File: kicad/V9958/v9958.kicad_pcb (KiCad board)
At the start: 2 copper layers, 160 x 100.3 mm, 5 parts, among them P5 CONN_02X25

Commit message: rca jacks, rough layout test
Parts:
- added C1: 22p, Capacitors_ThroughHole:C_Disc_D3_P2.5, F.Cu at (141.0, 97.8)
- added C10: 100n, Capacitors_ThroughHole:C_Disc_D3_P2.5, F.Cu at (179.1, 109.2)
- added C11: 47µF, Capacitors_ThroughHole:C_Radial_D5_L11_P2.5, F.Cu at (128.3, 105.4)
- added C12: 100n, Capacitors_ThroughHole:C_Disc_D3_P2.5, F.Cu at (179.1, 111.8)
- added C13: 100n, Capacitors_ThroughHole:C_Disc_D3_P2.5, F.Cu at (128.3, 101.6)
- added C14: 220µF, Capacitors_ThroughHole:C_Radial_D6.3_L11.2_P2.5, F.Cu at (85.1, 120.7)
- added C15: 220µF, Capacitors_ThroughHole:C_Radial_D6.3_L11.2_P2.5, F.Cu at (85.1, 78.7)
- added C16: 220µF, Capacitors_ThroughHole:C_Radial_D6.3_L11.2_P2.5, F.Cu at (85.1, 128.3)
- added C17: 47µF, Capacitors_ThroughHole:C_Radial_D5_L11_P2.5, F.Cu at (110.5, 81.3)
- added C18: 220µF, Capacitors_ThroughHole:C_Radial_D6.3_L11.2_P2.5, F.Cu at (85.1, 109.2)
- added C19: 100n, Capacitors_ThroughHole:C_Disc_D3_P2.5, F.Cu at (113.0, 86.4)
- added C2: 22p, Capacitors_ThroughHole:C_Disc_D3_P2.5, F.Cu at (141.0, 82.5)
- added C20: 220µF, Capacitors_ThroughHole:C_Radial_D6.3_L11.2_P2.5, F.Cu at (85.1, 63.5)
- added C21: 220µF, Capacitors_ThroughHole:C_Radial_D6.3_L11.2_P2.5, F.Cu at (85.1, 94.0)
- added C3: 100n, Capacitors_ThroughHole:C_Disc_D3_P2.5, F.Cu at (147.3, 80.0)
- added C4: 100n, Capacitors_ThroughHole:C_Disc_D3_P2.5, F.Cu at (160.0, 80.0)
- added C5: 100n, Capacitors_ThroughHole:C_Disc_D3_P2.5, F.Cu at (172.7, 80.0)
- added C6: 100n, Capacitors_ThroughHole:C_Disc_D3_P2.5, F.Cu at (185.4, 80.0)
- added C7: 100n, Capacitors_ThroughHole:C_Disc_D3_P2.5, F.Cu at (208.3, 108.0)
- added C8: 100n, Capacitors_ThroughHole:C_Disc_D3_P2.5, F.Cu at (158.8, 87.6)
- added C9: 100n, Capacitors_ThroughHole:C_Disc_D3_P2.5, F.Cu at (179.1, 114.3)
- added JP1: JUMPER, Pin_Headers:Pin_Header_Straight_1x02, F.Cu at (210.8, 91.4)
- added P1: RCA JACK, w_conn_av:rca_black, F.Cu at (71.1, 78.7)
- added P2: RCA JACK, w_conn_av:rca_black, F.Cu at (71.1, 109.2)
- added P3: RCA JACK, w_conn_av:rca_black, F.Cu at (71.1, 63.5)
- added P4: RCA JACK, w_conn_av:rca_black, F.Cu at (71.1, 94.0)
- added R1: 470, Resistors_ThroughHole:Resistor_Horizontal_RM10mm, F.Cu at (186.7, 119.4)
- added R10: 2.61k/10%, Resistors_ThroughHole:Resistor_Horizontal_RM10mm, F.Cu at (120.7, 82.5)
- added R11: 75, Resistors_ThroughHole:Resistor_Horizontal_RM10mm, F.Cu at (99.1, 124.5)
- added R12: 75, Resistors_ThroughHole:Resistor_Horizontal_RM10mm, F.Cu at (99.1, 120.7)
- added R13: 240, Resistors_ThroughHole:Resistor_Horizontal_RM10mm, F.Cu at (90.2, 96.5)
- added R2: 470, Resistors_ThroughHole:Resistor_Horizontal_RM10mm, F.Cu at (182.9, 119.4)
- added R3: 470, Resistors_ThroughHole:Resistor_Horizontal_RM10mm, F.Cu at (190.5, 119.4)
- added R4: 2.2k, Resistors_ThroughHole:Resistor_Horizontal_RM10mm, F.Cu at (124.5, 105.4)
- added R5: 2.2k, Resistors_ThroughHole:Resistor_Horizontal_RM10mm, F.Cu at (137.2, 104.1)
- added R6: 75, Resistors_ThroughHole:Resistor_Horizontal_RM10mm, F.Cu at (101.0, 78.7)
- added R7: 75, Resistors_ThroughHole:Resistor_Horizontal_RM10mm, F.Cu at (100.3, 109.2)
- added R8: 75, Resistors_ThroughHole:Resistor_Horizontal_RM10mm, F.Cu at (100.3, 63.5)
- added R9: 43, Resistors_ThroughHole:Resistor_Horizontal_RM10mm, F.Cu at (100.3, 92.7)
- added U1: 7400, Housings_DIP:DIP-14_W7.62mm_LongPads, F.Cu at (200.7, 111.8)
- added U2: V9958, SDIP:SDIP64, F.Cu at (175.3, 94.0)
- added U3: DRAM_64KX4, Housings_DIP:DIP-18_W7.62mm_LongPads, F.Cu at (147.3, 55.9)
- added U4: DRAM_64KX4, Housings_DIP:DIP-18_W7.62mm_LongPads, F.Cu at (160.0, 55.9)
- added U5: DRAM_64KX4, Housings_DIP:DIP-18_W7.62mm_LongPads, F.Cu at (172.7, 55.9)
- added U6: DRAM_64KX4, Housings_DIP:DIP-18_W7.62mm_LongPads, F.Cu at (185.4, 55.9)
- added U7: cxa2075M, Housings_SOIC:SOIC-24_7.5x15.4mm_Pitch1.27mm, F.Cu at (118.1, 94.0)
- added X1: OSC, Oscillators:KXO-200_LargePads, F.Cu at (116.8, 115.6)
- added X2: MINI_DIN_4, mini_din:mini_din-M_DIN4, F.Cu at (66.0, 124.5)
- added Y1: 21,443Mhz, Crystals:Crystal_HC49-U_Vertical, F.Cu at (142.2, 90.2)
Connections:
- net /CSW_VDP renamed /50pin connector/A5
- net /CS_RES02 renamed /CS_IO1
- net /Connector/A2 renamed /50pin connector/A2
- net /Connector/A3 renamed /50pin connector/A3
- net /Connector/A4 renamed /50pin connector/A4
- net /Connector/D0 renamed Net-(P5-Pad14)
- net /WE2 renamed /50pin connector/RESET_TRIG
- net E_LCD renamed /CS_IO0
- net Net-(P5-Pad19) renamed /CS_IO2
- P5 pad 10: /Connector/D4 -> /50pin connector/D3
- P5 pad 11: /Connector/D3 -> /50pin connector/D2
- P5 pad 12: /Connector/D2 -> /50pin connector/D1
- P5 pad 13: /Connector/D1 -> /50pin connector/D0
- P5 pad 15: Net-(P5-Pad15) -> /RW
- P5 pad 16: /RW -> Net-(P5-Pad16)
- P5 pad 17: Net-(P5-Pad17) -> RDY
- P5 pad 18: RDY -> Net-(P5-Pad18)
- P5 pad 24: /CSR_VDP -> /CS_VDP
- P5 pad 29: /Connector/A1 -> /50pin connector/A1
- P5 pad 30: /Connector/A0 -> /50pin connector/A0
- P5 pad 35: PHI2 -> GND
- P5 pad 36: Net-(P5-Pad36) -> PHI2
- P5 pad 37: /OE2 -> GND
- P5 pad 43: Net-(P5-Pad43) -> VCC
- P5 pad 44: Net-(P5-Pad44) -> VCC
- P5 pad 45: Net-(P5-Pad45) -> VCC
- P5 pad 46: Net-(P5-Pad46) -> VCC
- P5 pad 47: Net-(P5-Pad47) -> GND
- P5 pad 48: Net-(P5-Pad48) -> GND
- P5 pad 49: Net-(P5-Pad49) -> GND
- P5 pad 50: Net-(P5-Pad50) -> GND
- P5 pad 6: Net-(P5-Pad6) -> /50pin connector/D7
- P5 pad 7: /Connector/D7 -> /50pin connector/D6
- P5 pad 8: /Connector/D6 -> /50pin connector/D5
- P5 pad 9: /Connector/D5 -> /50pin connector/D4
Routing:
- net //CAS1: track 0.00 -> 64.1 mm, vias 0 -> 2
- net //RAS: track 0.00 -> 61.2 mm
- net /50pin connector/D7: track 0.00 -> 46.9 mm, vias 0 -> 1
- net /A2: track 0.00 -> 41.3 mm
- net /50pin connector/A1: track 0.00 -> 41.3 mm
- net /50pin connector/A0: track 0.00 -> 41.3 mm
- net /A3: track 0.00 -> 41.2 mm
- net /A5: track 0.00 -> 41.2 mm
- net /A7: track 0.00 -> 41.1 mm
- net /A6: track 0.00 -> 41.0 mm
- net /R/W: track 0.00 -> 41.0 mm
- net /A4: track 0.00 -> 41.0 mm
- net //CAS0: track 0.00 -> 38.2 mm
- net /50pin connector/D1: track 0.00 -> 30.9 mm, vias 0 -> 1
- net /50pin connector/D3: track 0.00 -> 30.0 mm, vias 0 -> 1
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
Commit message: cleanup
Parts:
- P1: value RCA JACK -> RED
- P2: value RCA JACK -> GREEN
- P3: value RCA JACK -> BLUE
- P4: value RCA JACK -> SYNC/C
- R1, R10, R11, R12, R13, R2, R3, R4, R5, R6, R7, R8, R9: footprint Resistors_ThroughHole:Resistor_Horizontal_RM10mm -> Discret:R3
- moved C11 85.4 mm to (95.2, 184.2)
- moved C13 85.4 mm to (95.2, 180.3)
- moved C19 85.4 mm to (80.0, 165.1)
- moved R10 85.4 mm to (87.6, 161.3)
- moved R4 85.4 mm to (91.4, 184.2)
- moved C17 82.5 mm to (96.5, 162.6)
- moved C10 81.3 mm to (115.6, 160.0)
- moved C12 81.3 mm to (115.6, 162.6)
- moved C9 81.3 mm to (115.6, 165.1)
- moved R1 81.3 mm to (123.2, 170.2)
- moved R2 81.3 mm to (119.4, 170.2)
- moved R3 81.3 mm to (127.0, 170.2)
- moved C4 49.1 mm to (111.8, 88.9)
- moved C5 49.1 mm to (124.5, 88.9)
- moved C3 49.1 mm to (99.1, 88.9)
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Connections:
- net /A2 renamed /AD2
- net /A3 renamed /AD3
- net /A4 renamed /AD4
- net /A5 renamed /AD5
- net /A6 renamed /AD6
- net /A7 renamed /AD7
- U2 pad 49: /50pin connector/A0 -> /AD0
- U2 pad 50: /50pin connector/A1 -> /AD1
- U3 pad 13: /50pin connector/A1 -> /AD1
- U3 pad 14: /50pin connector/A0 -> /AD0
- U4 pad 13: /50pin connector/A1 -> /AD1
- U4 pad 14: /50pin connector/A0 -> /AD0
- U5 pad 13: /50pin connector/A1 -> /AD1
- U5 pad 14: /50pin connector/A0 -> /AD0
- U6 pad 13: /50pin connector/A1 -> /AD1
- U6 pad 14: /50pin connector/A0 -> /AD0
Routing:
- net VCC: track 10.0 -> 99.8 mm
- net /AD1: track 0.00 -> 83.8 mm, vias 0 -> 1
- net /AD0: track 0.00 -> 82.2 mm, vias 0 -> 1
- net /RESET: track 0.00 -> 64.3 mm, vias 0 -> 1
- net /AD4: track 41.0 -> 88.7 mm, vias 0 -> 1
- net /AD5: track 41.2 -> 85.0 mm, vias 0 -> 1
- net /AD2: track 41.3 -> 84.1 mm, vias 0 -> 1
- net /AD3: track 41.2 -> 83.9 mm, vias 0 -> 1
- net /AD6: track 41.0 -> 81.6 mm, vias 0 -> 1
- net /IRQ: track 0.00 -> 38.7 mm, vias 0 -> 1
- net /AD7: track 41.1 -> 78.5 mm, vias 0 -> 1
- net //CAS1: track 64.1 -> 28.5 mm, vias 2 -> 0
- net /R/W: track 41.0 -> 70.8 mm
- net /50pin connector/D7: track 46.9 -> 18.3 mm, vias 1 -> 0
- net /RD1: track 28.5 -> 0.00 mm
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
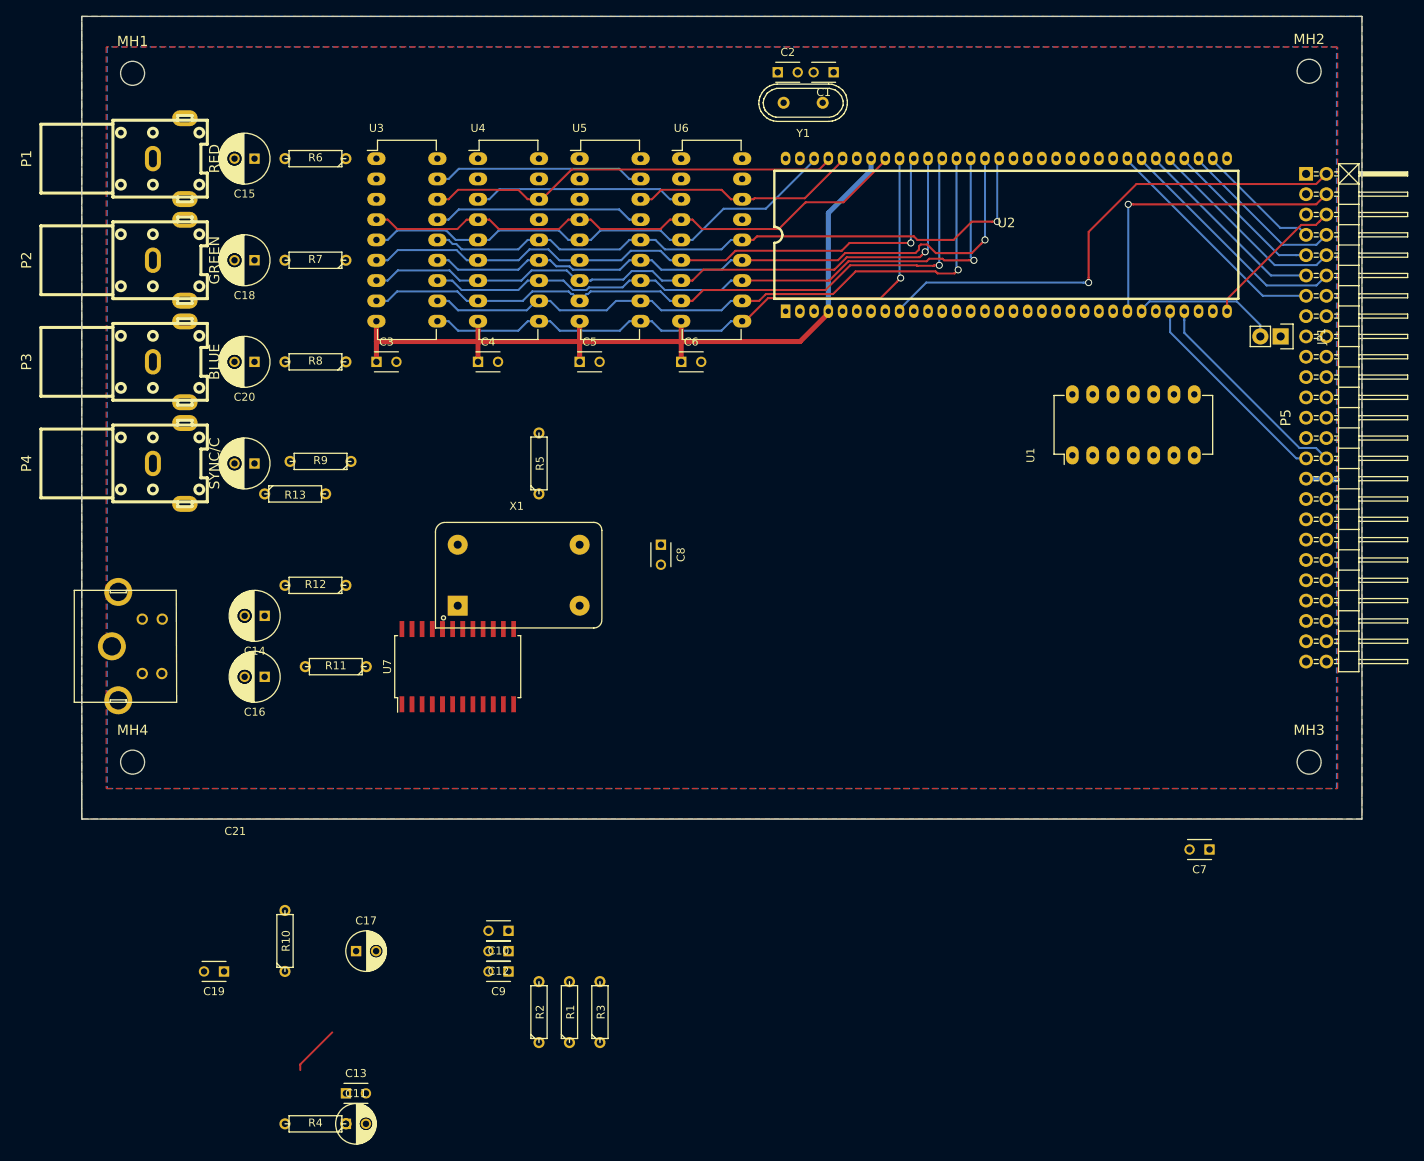
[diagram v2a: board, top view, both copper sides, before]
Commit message: 74139 instead of 7400
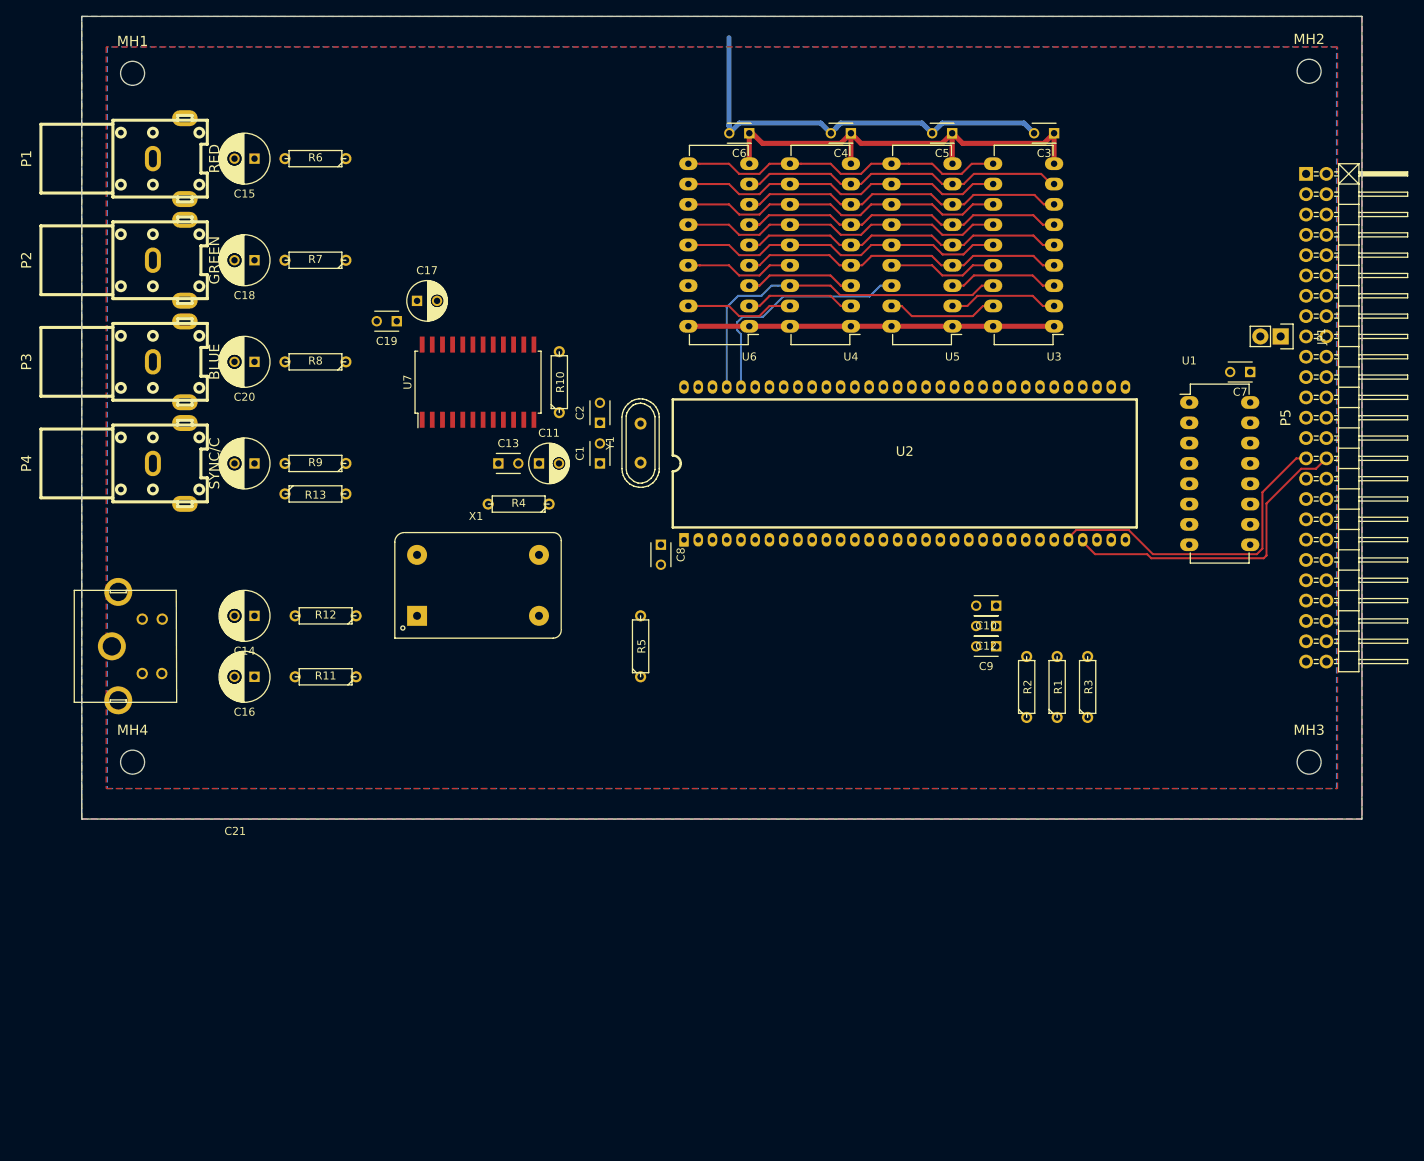
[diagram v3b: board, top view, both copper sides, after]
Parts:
- U1: value 7400 -> 74LS139; footprint Housings_DIP:DIP-14_W7.62mm_LongPads -> Housings_DIP:DIP-16_W7.62mm_LongPads
- X2: value MINI_DIN_4 -> S-VIDEO
- moved C3 89.4 mm to (183.8, 60.3), turned to 180 degrees
- moved U3 87.3 mm to (183.8, 84.5), turned to 180 degrees
- moved C11 86.0 mm to (119.4, 101.6)
- moved C19 84.1 mm to (101.6, 83.8)
- moved C17 81.6 mm to (104.1, 81.3)
- moved R4 81.5 mm to (116.8, 106.7)
- moved C13 81.0 mm to (114.3, 101.6)
- moved R10 77.8 mm to (121.9, 91.4)
- moved C10 73.3 mm to (176.5, 119.4)
- moved C12 73.3 mm to (176.5, 121.9)
- moved C9 73.3 mm to (176.5, 124.5)
- moved R1 73.3 mm to (184.2, 129.5)
- moved R2 73.3 mm to (180.3, 129.5)
- moved R3 73.3 mm to (188.0, 129.5)
- moved C7 59.9 mm to (208.3, 90.2)
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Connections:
- C11 pad 1: Net-(C11-Pad1) -> VCC
- C12 pad 1: /RGB_R -> /RGB_B
- C13 pad 1: Net-(C13-Pad1) -> VCC
- C17 pad 1: Net-(C17-Pad1) -> VCC
- C19 pad 1: Net-(C19-Pad1) -> VCC
- C9 pad 1: /RGB_B -> /RGB_R
- R1 pad 2: /RGB_R -> /RGB_G
- R2 pad 2: /RGB_G -> /RGB_R
- U1 pad 1: /RW -> /CS_VDP
- U1 pad 10: Net-(U1-Pad10) -> (no net)
- U1 pad 11: Net-(U1-Pad11) -> (no net)
- U1 pad 12: Net-(U1-Pad12) -> (no net)
- U1 pad 13: /RW -> (no net)
- U1 pad 14: VCC -> (no net)
- U1 pad 3: Net-(U1-Pad10) -> GND
- U1 pad 4: /CS_VDP -> Net-(U1-Pad4)
- U1 pad 5: /CS_VDP -> Net-(U1-Pad5)
- U1 pad 6: Net-(U1-Pad12) -> Net-(U1-Pad6)
- U1 pad 7: GND -> Net-(U1-Pad7)
- U1 pad 8: Net-(U1-Pad8) -> GND
- U1 pad 9: Net-(U1-Pad12) -> (no net)
- U2 pad 30: Net-(U1-Pad8) -> Net-(U1-Pad4)
- U2 pad 31: Net-(U1-Pad11) -> Net-(U1-Pad5)
- U3 pad 18: VSS -> GND
- U4 pad 18: VSS -> GND
- U5 pad 18: VSS -> GND
- U6 pad 18: VSS -> GND
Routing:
- net GND: track 3.99 -> 99.2 mm
- net /RESET: track 64.3 -> 0.00 mm, vias 1 -> 0
- net /AD4: track 88.7 -> 41.3 mm, vias 1 -> 0
- net /AD5: track 85.0 -> 41.2 mm, vias 1 -> 0
- net /AD2: track 84.1 -> 41.3 mm, vias 1 -> 0
- net /AD3: track 83.9 -> 41.3 mm, vias 1 -> 0
- net /AD1: track 83.8 -> 41.3 mm, vias 1 -> 0
- net VCC: track 99.8 -> 58.3 mm
- net /AD0: track 82.2 -> 41.2 mm, vias 1 -> 0
- net /AD6: track 81.6 -> 41.0 mm, vias 1 -> 0
- net /IRQ: track 38.7 -> 0.00 mm, vias 1 -> 0
- net /AD7: track 78.5 -> 41.3 mm, vias 1 -> 0
- net /50pin connector/D1: track 30.3 -> 0.00 mm
- net /R/W: track 70.8 -> 41.1 mm
- net /50pin connector/D0: track 29.6 -> 0.00 mm
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
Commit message: layout complete, still needs polish
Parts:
- moved R1 15.3 mm to (174.0, 118.1)
- moved R3 14.5 mm to (179.1, 118.1)
- moved R5 13.5 mm to (141.0, 114.3), turned to 180 degrees
- moved R2 12.0 mm to (176.5, 118.1)
- moved C8 9.92 mm to (142.2, 105.4), turned to 180 degrees
- moved C9 9.16 mm to (171.4, 116.8)
- moved C19 7.73 mm to (109.2, 82.5)
- moved C13 7.41 mm to (120.7, 97.8)
- moved C10 7.18 mm to (171.4, 114.3)
- moved R4 6.73 mm to (111.1, 103.1), turned to 90 degrees
- moved C12 5.68 mm to (171.4, 119.4)
- moved C11 1.27 mm to (120.7, 101.6)
- moved C17 1.27 mm to (104.1, 82.5), turned to 180 degrees
- turned R10 to 270 degrees
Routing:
- net GND: track 99.2 -> 552.8 mm, vias 0 -> 1
- net VCC: track 58.3 -> 371.5 mm
- net /RESET: track 0.00 -> 88.1 mm
- net Net-(C9-Pad2): track 0.00 -> 75.5 mm
- net Net-(C12-Pad2): track 0.00 -> 73.2 mm
- net Net-(C10-Pad2): track 0.00 -> 71.5 mm
- net /IRQ: track 0.00 -> 61.9 mm
- net Net-(R11-Pad1): track 0.00 -> 57.1 mm
- net /50pin connector/D7: track 0.00 -> 52.1 mm
- net Net-(R12-Pad1): track 0.00 -> 47.0 mm
- net Net-(JP1-Pad2): track 0.00 -> 46.8 mm
- net /50pin connector/D5: track 0.00 -> 46.6 mm, vias 0 -> 1
- net /50pin connector/D3: track 0.00 -> 45.9 mm, vias 0 -> 1
- net /50pin connector/D1: track 0.00 -> 43.2 mm, vias 0 -> 1
- net /50pin connector/D4: track 0.00 -> 43.1 mm, vias 0 -> 1
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- added copper zone on F.Cu, net GND

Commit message: cleanup, make productiom ready
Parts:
- U1: value 74LS139 -> 74HCT139
- moved R11 31.8 mm to (91.4, 96.5)
- moved R12 21.6 mm to (91.4, 99.1)
- moved R6 20.3 mm to (91.4, 83.8)
- moved R13 11.4 mm to (91.4, 94.0), turned to 180 degrees
- moved C8 10.9 mm to (148.6, 96.5)
- moved R7 10.2 mm to (91.4, 86.4)
- moved R9 10.2 mm to (91.4, 91.4)
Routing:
- net Net-(C16-Pad1): track 5.08 -> 39.0 mm
- net Net-(R11-Pad1): track 57.1 -> 24.1 mm
- net GND: track 552.8 -> 576.9 mm
- net Net-(C14-Pad1): track 5.08 -> 26.1 mm
- net Net-(R12-Pad1): track 47.0 -> 26.8 mm
- net Net-(C15-Pad1): track 3.81 -> 23.2 mm
- net Net-(R6-Pad1): track 30.6 -> 14.0 mm
- net Net-(C21-Pad1): track 7.62 -> 20.4 mm
- net /50pin connector/D6: track 43.0 -> 34.4 mm
- net /50pin connector/D5: track 46.6 -> 38.6 mm
- net Net-(C18-Pad1): track 3.81 -> 11.8 mm
- net VCC: track 371.5 -> 364.5 mm
- net /50pin connector/D4: track 43.1 -> 36.8 mm
- net /50pin connector/D3: track 45.9 -> 40.3 mm
- net Net-(R9-Pad1): track 21.2 -> 17.4 mm
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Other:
- board text added: "Steckschwein V9958/Video Board v0.1 2018 Thomas Woinke / Marko Lauke http://www.steckschwein.de/"
